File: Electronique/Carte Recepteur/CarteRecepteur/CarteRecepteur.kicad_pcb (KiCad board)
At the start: 2 copper layers, 36 x 50 mm, 5 parts, among them J1 Conn_02x04_Odd_Even_MountingP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

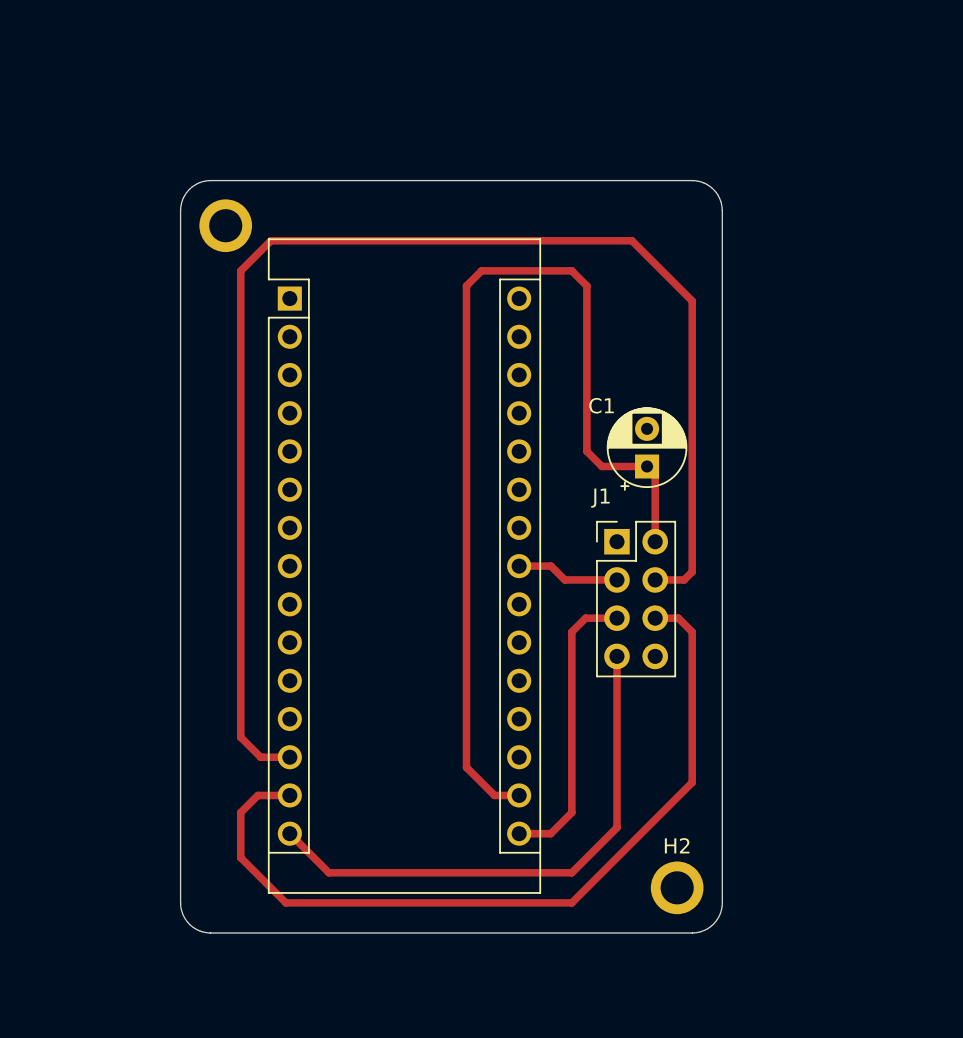
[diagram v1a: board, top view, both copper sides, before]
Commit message: Modif Control Rotation
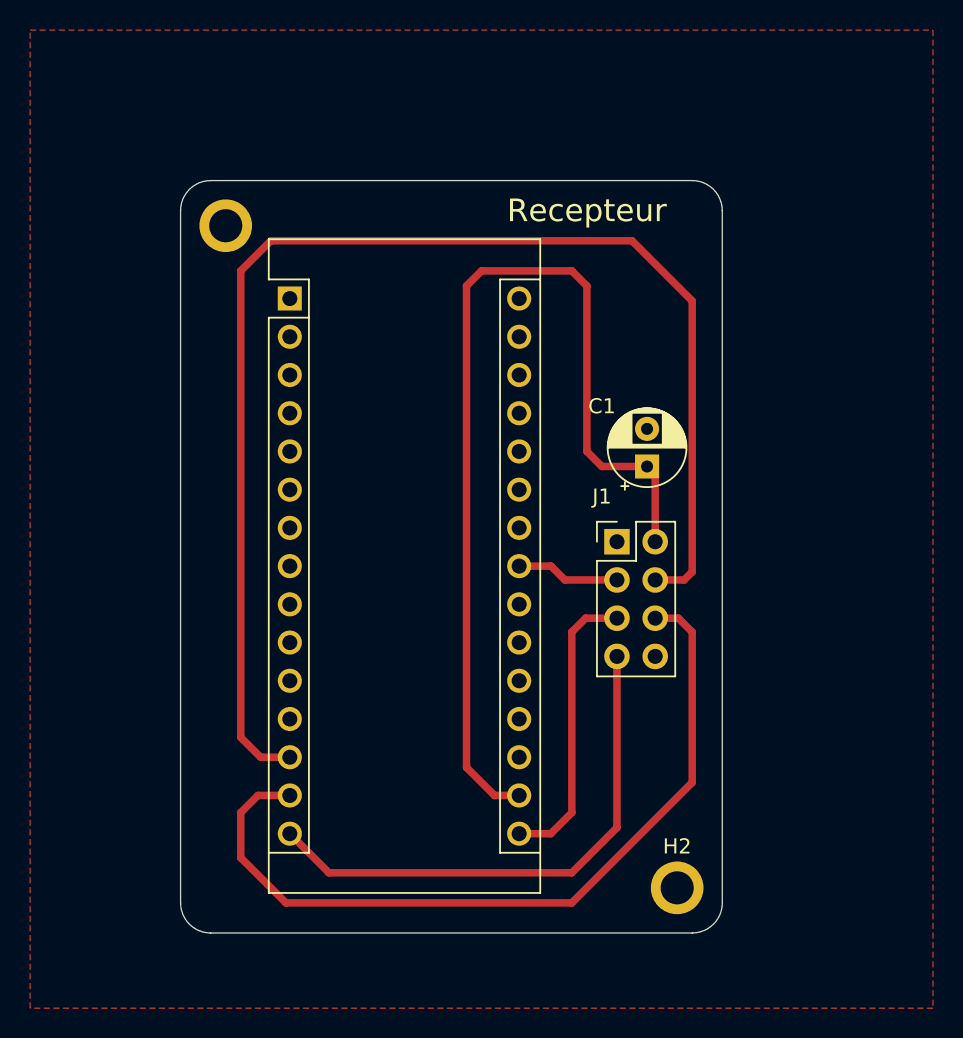
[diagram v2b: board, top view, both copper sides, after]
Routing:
- added copper zone on F.Cu, net GND
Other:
- board text added: "Recepteur"
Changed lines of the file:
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@@
   (general
     (thickness 1.6)
-    (drawings 11)
+    (drawings 12)
     (tracks 41)
     (zones 0)
@@
       (outputformat 1)
       (mirror false)
-      (drillshape 1)
+      (drillshape 0)
       (scaleselection 1)
-      (outputdirectory ""))
+      (outputdirectory "gerbers/"))
   )
   (net 0 "")
@@
     )
   )
+  (gr_text Recepteur (at 132 47) (layer F.SilkS)
+    (effects (font (size 1.5 1.5) (thickness 0.3)))
+  )
   (dimension 44 (width 0.15) (layer Dwgs.User)
     (gr_text "44,000 mm" (at 103.3 70 90) (layer Dwgs.User)
@@
   (segment (start 130.54 71.54) (end 134 71.54) (width 0.5) (layer F.Cu) (net 7))
   (segment (start 129.62 70.62) (end 130.54 71.54) (width 0.5) (layer F.Cu) (net 7))
+  (zone (net 5) (net_name GND) (layer F.Cu) (hatch edge 0.508)
+    (connect_pads (clearance 0.508))
+    (min_thickness 0.254)
+    (fill yes (arc_segments 32) (thermal_gap 0.508) (thermal_bridge_width 0.508))
+    (polygon
+      (pts
+        (xy 155 100) (xy 95 100) (xy 95 35) (xy 155 35)
+      )
+    )
+  )
 )

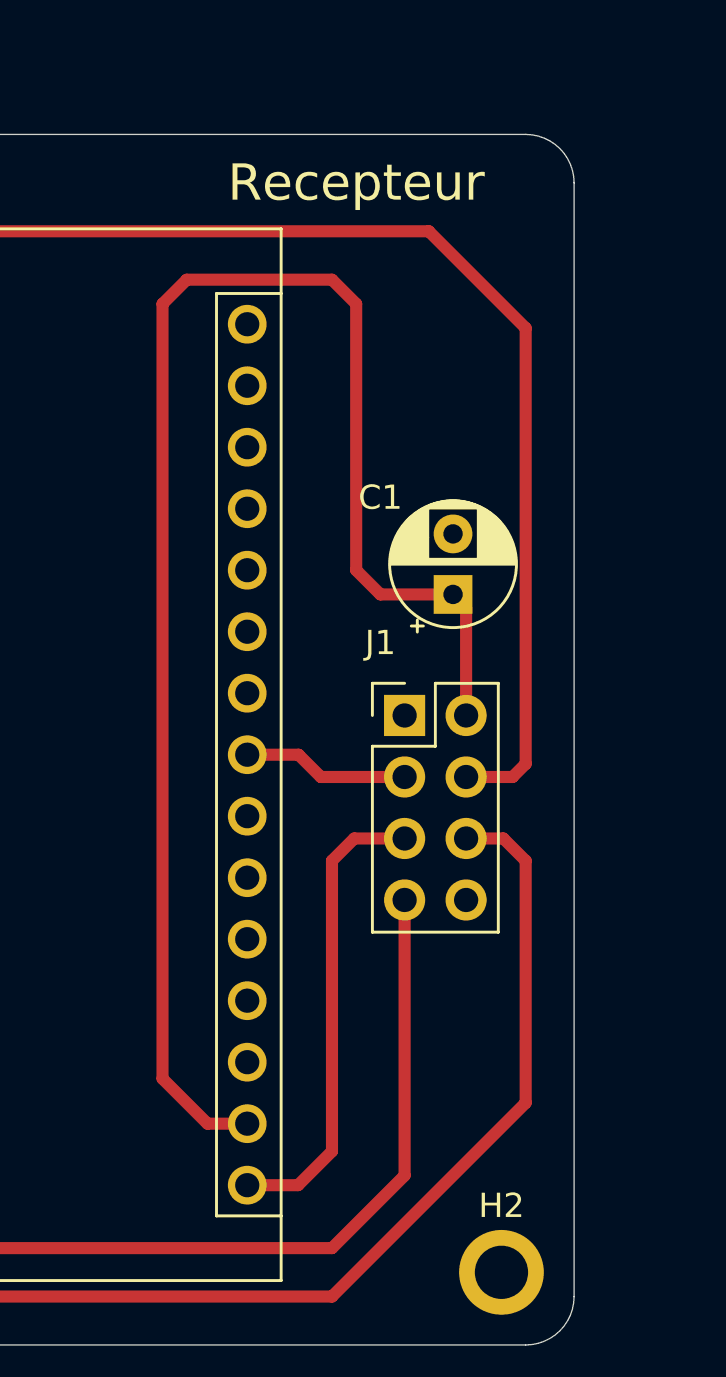
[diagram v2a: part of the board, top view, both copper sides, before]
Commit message: ajout d'une FIFO pour le module nRF
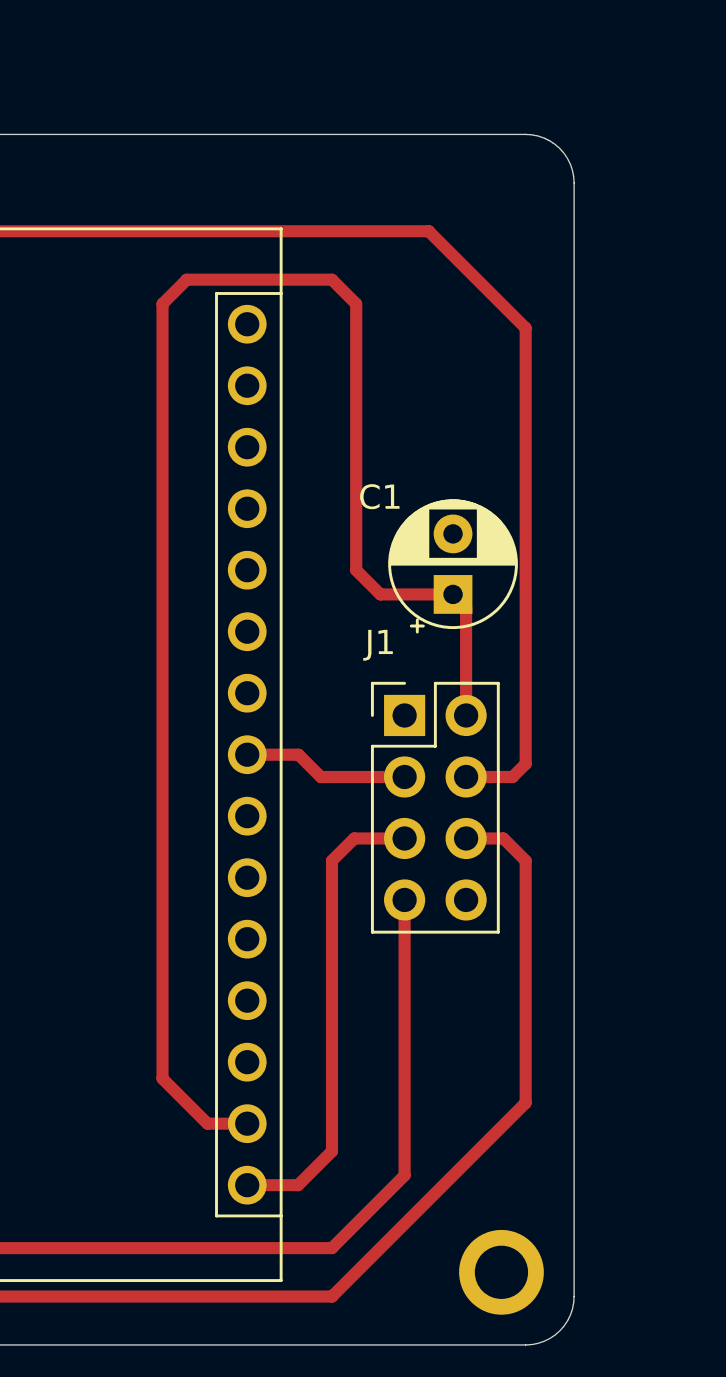
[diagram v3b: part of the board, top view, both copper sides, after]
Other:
- board text added: "Ares ENSEA"
- board text added: "Bottom"
- board text added: "Top"
